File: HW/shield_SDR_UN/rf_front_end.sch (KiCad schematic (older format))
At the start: 1 part, among them U1 MAX5864

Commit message: ADC schematic done.
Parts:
- added C1: 100nF, symbol Device:C
- added C10, C4, C8, C9: 0.47uF, symbol Device:C
- added C2: 10uF, symbol Device:C
- added C3, C5, C6, C7: 4.7uF, symbol Device:C
- added CA1, CA2, CA3: 330nF, symbol Device:C
- added D1: LED, symbol Device:LED
- added FB1: FILTER, symbol hackrf-one-packages:FILTER
- added Q1: MOSFET_P, symbol hackrf-one-packages:MOSFET_P
- added R1: 10k, symbol Device:R
- added R2: 1.8k, symbol Device:R
- U1: symbol hack-packages:MAX5864 -> quacho-packages:MAX5864
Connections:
- net labels added: !VAA_ENABLE, COM, IA+, IA-, ID+, ID-, QA+, QA-, QD+, QD-, REFN, REFP, VAA, VCC, adCLK, adCS, adCSK, adDA0, adDA1, adDA2, adDA3, adDA4, adDA5, adDA6, adDA7, adDD0, adDD1, adDD2, adDD3, adDD4, adDD5, adDD6, adDD7, adDD8, adDD9, adMOSI
- wire segments 5 -> 108
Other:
- note added: "Revisar si la tierra del pin 17\nOGND debe ser digital o análoga"
- note added: "U1-18 bypass\ncapacitors"
- note added: "U1-2,8,43 bypass\ncapacitors"

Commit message: proc schematic done test.
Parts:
- FB1: symbol hackrf-one-packages:FILTER -> shield_SDR_UN-rescue:FILTER-hackrf-one-packages
- Q1: symbol hackrf-one-packages:MOSFET_P -> shield_SDR_UN-rescue:MOSFET_P-hackrf-one-packages
- U1: symbol quacho-packages:MAX5864 -> shield_SDR_UN-rescue:MAX5864-quacho-packages
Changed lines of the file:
@@
 	6050 2200 6200 2200
 $Comp
-L quacho-packages:MAX5864 U1
+L shield_SDR_UN-rescue:MAX5864-quacho-packages U1
 U 1 1 5CCB83DB
 P 4850 2550
@@
 $EndComp
 $Comp
-L hackrf-one-packages:MOSFET_P Q1
+L shield_SDR_UN-rescue:MOSFET_P-hackrf-one-packages Q1
 U 1 1 5CCE48D1
 P 1350 1400
@@
 	850  1750 850  1600
 $Comp
-L hackrf-one-packages:FILTER FB1
+L shield_SDR_UN-rescue:FILTER-hackrf-one-packages FB1
 U 1 1 5CCED73E
 P 1250 2200
+AR Path="/5CCED73E" Ref="FB1"  Part="1"
+AR Path="/5CC081D2/5CCED73E" Ref="FB1"  Part="1"
 F 0 "FB1" V 1204 2302 50  0000 L CNN
 F 1 "FILTER" V 1295 2302 50  0000 L CNN

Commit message: MAX2830 Symbol/Footprint created
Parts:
- added C11, C13, C15: 2.2uF, symbol Device:C
- added C12, C14, C16: 100nF, symbol Device:C
- added R10, R7, R8, R9: 4.7k, symbol Device:R
- added R3, R4, R5, R6: 1k, symbol Device:R
- added U2: MAX2830, FP-MAX2830:MAX2830ETM&plus_, symbol quacho-packages:MAX2830
- C10, C8: value 0.47uF -> 100nF
- C4: renamed from C5; value 4.7uF -> 2.2uF
- C6: value 4.7uF -> 100nF
- C7: value 4.7uF -> 2.2uF
- C9: value 0.47uF -> 2.2uF
- FB1: symbol shield_SDR_UN-rescue:FILTER-hackrf-one-packages -> hackrf-one-packages:FILTER
- Q1: symbol shield_SDR_UN-rescue:MOSFET_P-hackrf-one-packages -> hackrf-one-packages:MOSFET_P
- U1: symbol shield_SDR_UN-rescue:MAX5864-quacho-packages -> quacho-packages:MAX5864
- renumbered C4 to C5, CA3 to CA1, CA1 to CA2, CA2 to CA3
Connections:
- wire segments 108 -> 159
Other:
- note added: "1%"
- note added: "ADC-18 bypass\ncapacitors"
- note added: "ADC-2,8,11,33,39,43,46 bypass capacitors"
- note removed: "U1-18 bypass\ncapacitors"
- note removed: "U1-2,8,43 bypass\ncapacitors"
- moved on the sheet: C10, C3, C4, C5, C6, C7, C8, C9

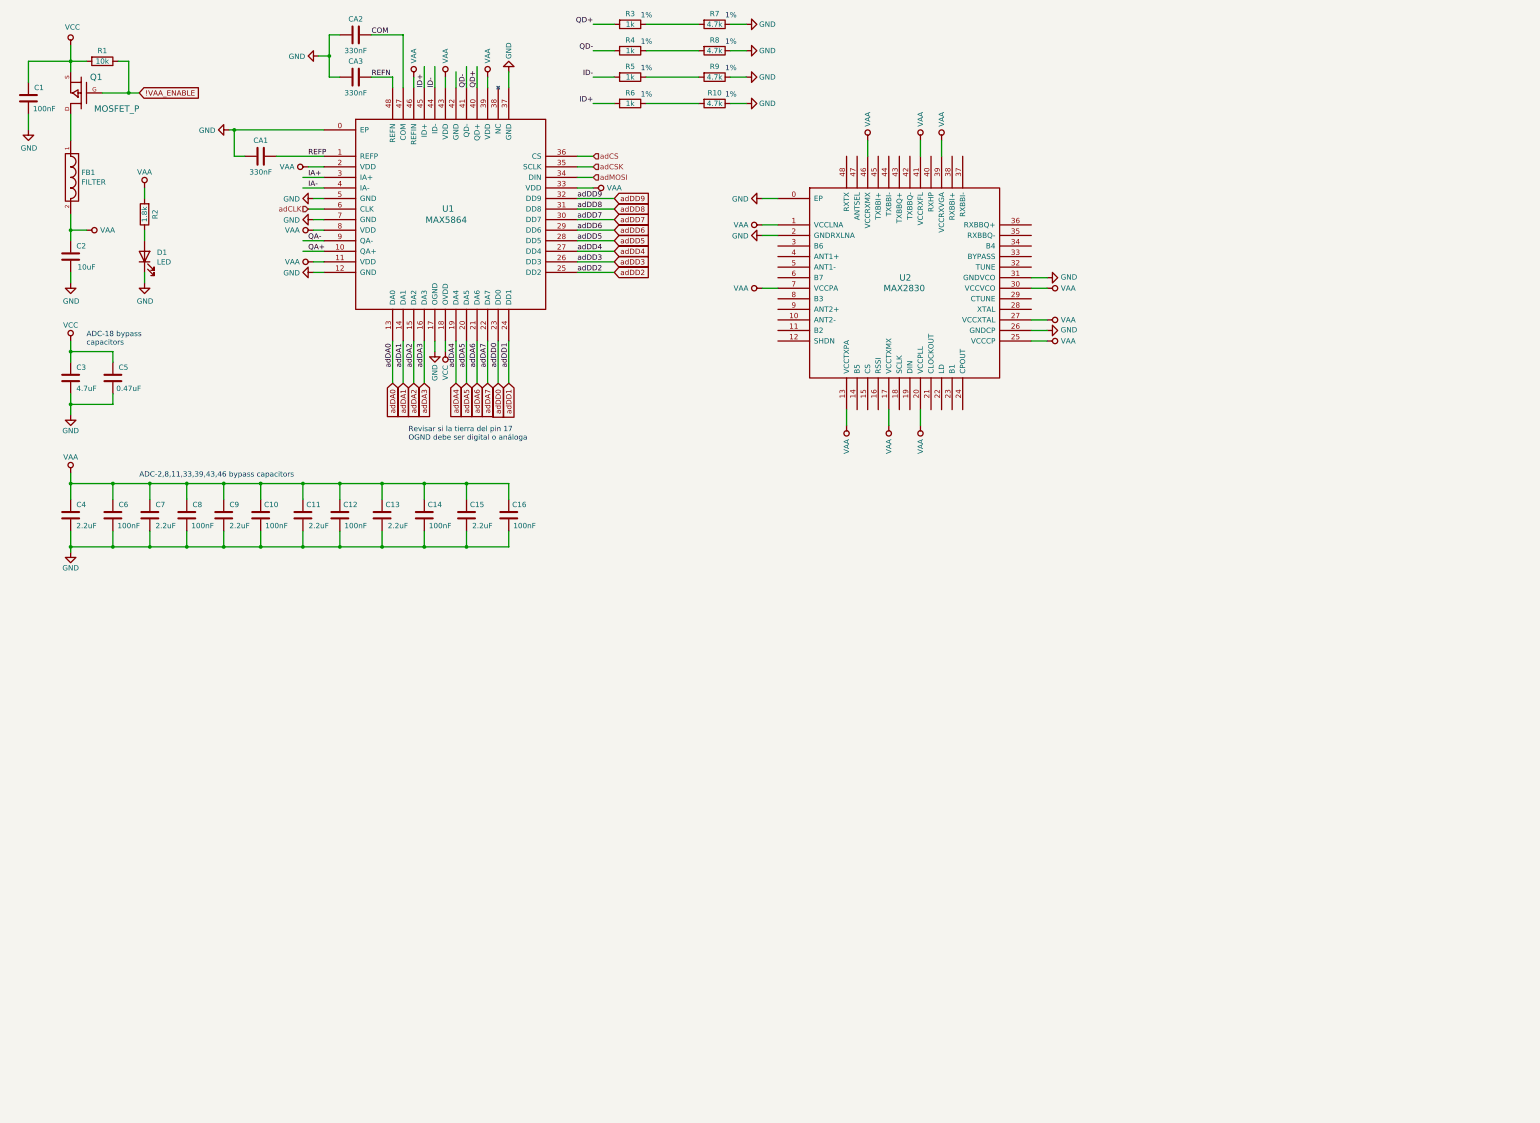
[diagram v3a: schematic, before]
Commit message: Onion 2 routed
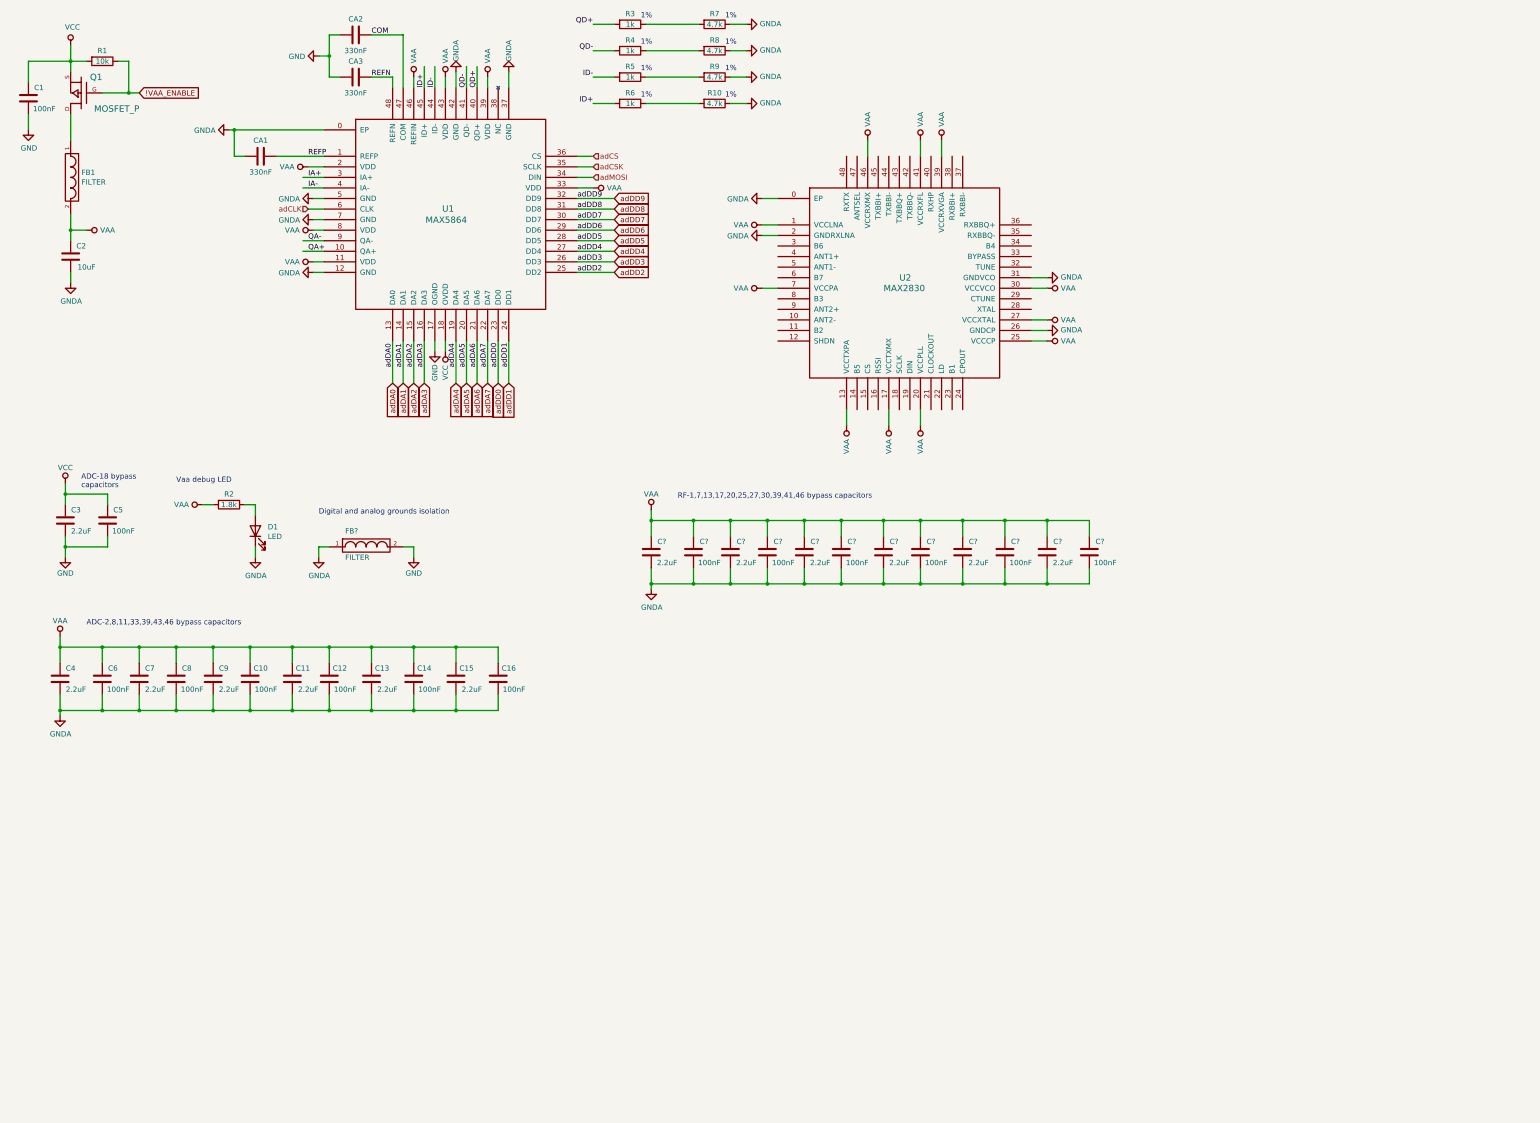
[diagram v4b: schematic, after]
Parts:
- added C? (x6): 2.2uF, symbol Device:C
- added C? (x6): 100nF, symbol Device:C
- added FB?: FILTER, symbol hackrf-one-packages:FILTER
- C3: value 4.7uF -> 2.2uF
- C5: value 0.47uF -> 100nF
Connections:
- net labels added: GNDA
- wire segments 159 -> 212
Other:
- note added: "Digital and analog grounds isolation"
- note added: "RF-1,7,13,17,20,25,27,30,39,41,46 bypass capacitors"
- note added: "Vaa debug LED"
- note removed: "Revisar si la tierra del pin 17\nOGND debe ser digital o análoga"
- moved on the sheet: C10, C11, C12, C13, C14, C15, C16, C3, C4, C5, C6, C7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

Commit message: RF-Frontend balun
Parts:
- added C?: 100nF, symbol Device:C
- added C? (x2): 0, symbol Device:C
- added P? (x2): GSG-RF-CONN, symbol hackrf-one-rescue:GSG-RF-CONN
- added R? (x4): 0, symbol Device:R
- added T? (x2): BALUN, symbol hackrf-one-rescue:BALUN
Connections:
- net labels added: RXBBI+, RXBBI-, RXBBQ+, RXBBQ-, TXBBI+, TXBBI-, TXBBQ+, TXBBQ-, rfB1, rfB2, rfB3, rfB4, rfB5, rfB6, rfB7
- wire segments 212 -> 261
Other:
- moved on the sheet: C10, C11, C12, C13, C14, C15, C16, C3, C4, C5, C6, C7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

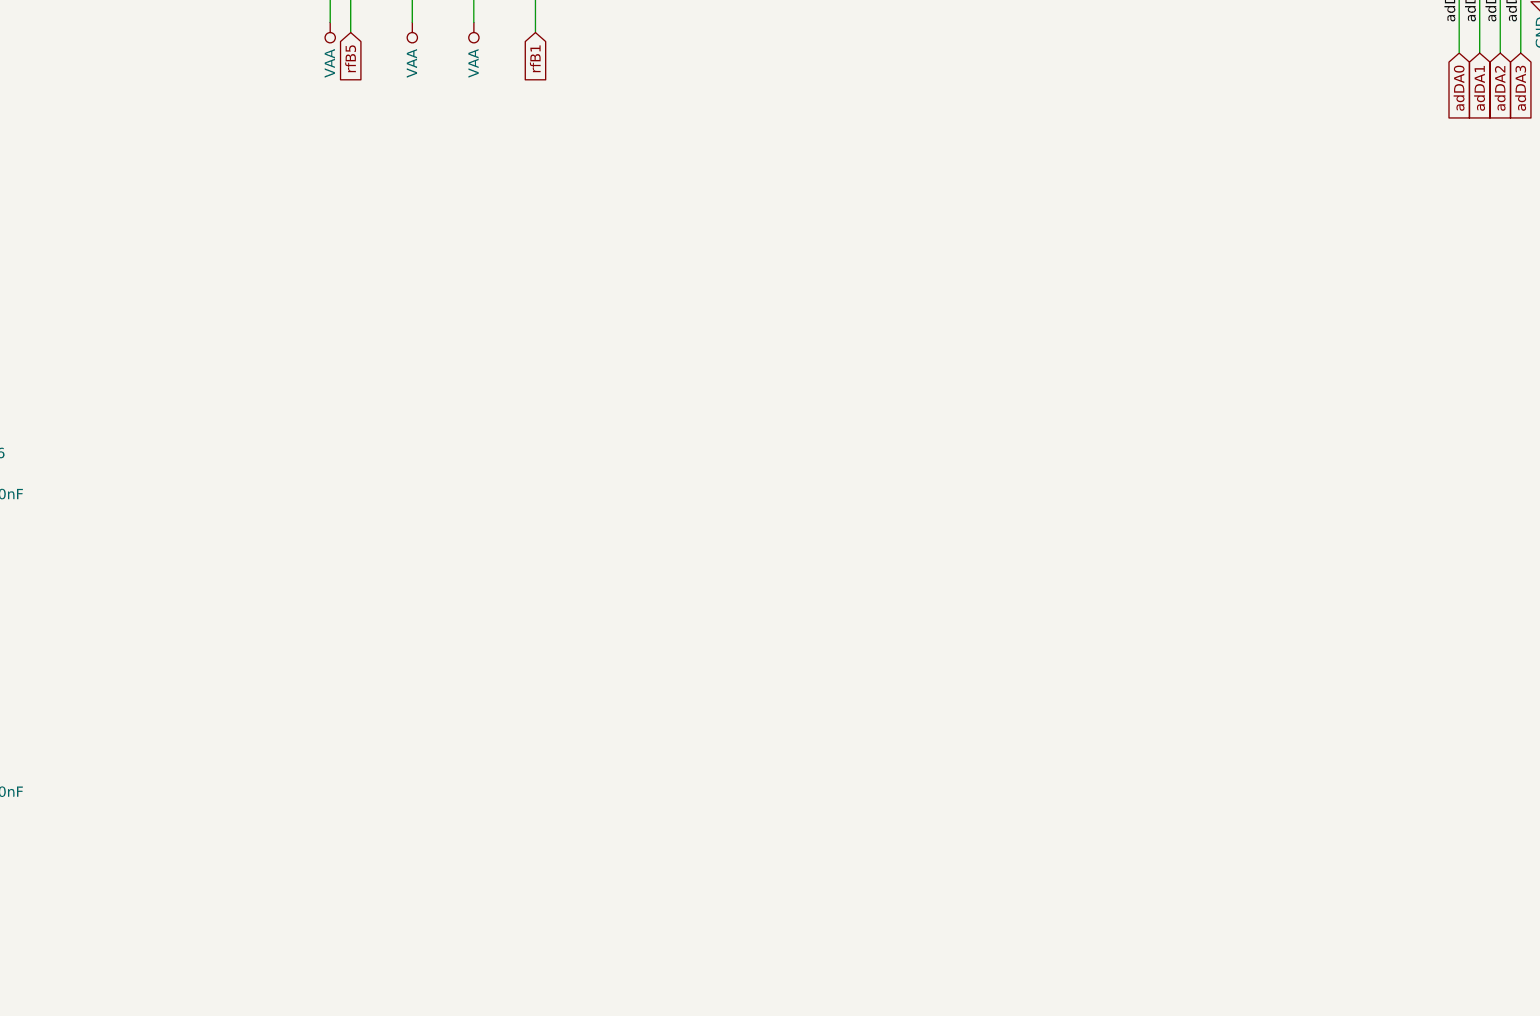
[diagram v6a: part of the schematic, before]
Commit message: se agrego el chip multirelojes
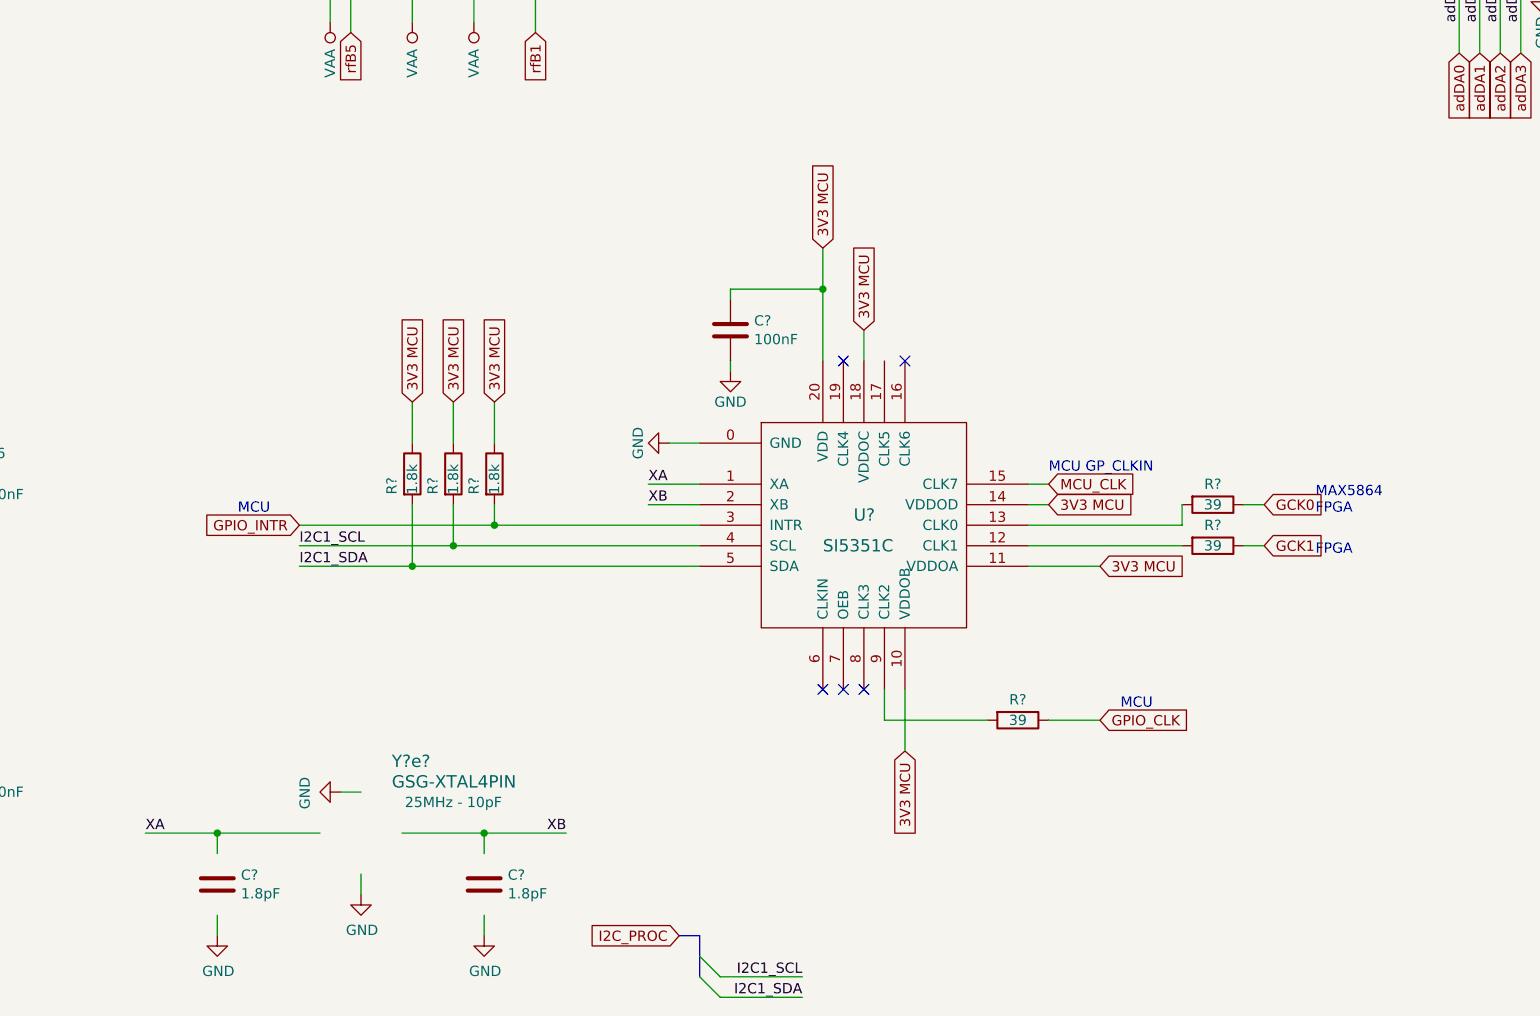
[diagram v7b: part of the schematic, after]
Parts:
- added C?: 100nF, Capacitor_SMD:C_0603_1608Metric_Pad1.05x0.95mm_HandSolder, symbol Device:C
- added C? (x2): 1.8pF, Capacitor_SMD:C_0603_1608Metric_Pad1.05x0.95mm_HandSolder, symbol Device:C
- added R? (x3): 39, Resistor_SMD:R_0402_1005Metric, symbol Device:R
- added R? (x3): 1.8k, Resistor_SMD:R_0603_1608Metric_Pad1.05x0.95mm_HandSolder, symbol Device:R
- added U?: SI5351C, symbol hackrf-one-rescue:SI5351C
- added Y?e?: GSG-XTAL4PIN, CRISTAL_4:GSG-XTAL3.2x2.5mm, symbol UL_ABM9G25000MHZB4YT:ABM8G-25.000MHZ-B4Y-T
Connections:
- net labels added: 3V3 MCU, GCK0, GCK1, GPIO_CLK, GPIO_INTR, I2C1_SCL, I2C1_SDA, I2C_PROC, MCU_CLK, XA, XB
- wire segments 261 -> 306
- no-connect marks 0 -> 5
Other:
- note added: "FPGA"
- note added: "MAX5864\nFPGA"
- note added: "MCU"
- note added: "MCU GP_CLKIN"
